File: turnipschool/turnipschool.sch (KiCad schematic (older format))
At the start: 45 parts, among them J1 GSG-900MHZ-F-ANTENNA, J2 GSG-USB-MICRO-B, P2 ANTENNA, P3 RESET_N, P4 DD, P5 DC, P6 3V3, P7 GND, P9 PWR, T1 BALUN, U1 CC1111, U2 AP7313, X1 CRYSTAL

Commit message: Add USB hub to TURNIPSCHOOL
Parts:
- removed J2: GSG-USB-MICRO-B, symbol GSG-USB-MICRO-B
- removed P9: PWR, symbol CONN_3X2
- added C15: 100uF, symbol C
- added C16: 100nF, symbol C
- added C17: 1uF, symbol C
- added C18, C19: 18pF, symbol C
- added J?: USB-DEVICE, symbol USB-DEVICE
- added P10, P11, P8, P9: CONN_1, symbol CONN_1
- added P8: GOODFET, symbol CONN_7X2
- added R14: 10k, symbol R
- added R15: 0, symbol R-SHORTED
- added R16, R17: 33, symbol R
- added R18, R19: 50k, symbol R
- added R20: 12k, symbol R
- added R21, R22, R23, R24: 100k, symbol R
- added U3: USB2412, symbol USB2412
- added U4: AP2511SN-7, symbol AP2511SN-7
- added X2: CRYSTAL, symbol CRYSTAL
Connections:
- net labels added: USBDM_DN2, USBDP_DN2
- wire segments 130 -> 189
- no-connect marks 1 -> 16
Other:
- note added: "programming header matching GoodFET pinout"
- moved on the sheet: C1, C10, C11, C12, C13, C14, C15, C16, C17, C2, C3, C4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

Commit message: Remove trace antenna, swap connector for pad
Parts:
- removed C6: 10nF, symbol C
- removed J1: GSG-900MHZ-F-ANTENNA, symbol GSG-900MHZ-F-ANTENNA
- removed P2: ANTENNA, symbol GSG-SMA-CONN
- added P13: CONN_1, symbol CONN_1
- C17: Note DNP -> (none)
- gave numbers to parts that had none: 1
- renumbered C15 to C20, C16 to C21, C17 to C22, P9 to P10, P10 to P11, P11 to P12, P8 to P9
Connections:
- wire segments 189 -> 181
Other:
- note added: "USB Cable"
- moved on the sheet: P10, P11, P12, P9

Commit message: Add changes suggestted by mossmann
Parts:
- removed C12, C13: 47pF, symbol C
- removed D1: TVS_DIODE, symbol GSG-DIODE-TVS-BI
- removed D3: LED2, symbol LED
- removed D4: LED3, symbol LED
- removed J2: USB-DEVICE, symbol USB-DEVICE
- removed P8: GOODFET, symbol CONN_7X2
- removed R11, R12: 330, symbol R
- removed R13, R15, R7: 0, symbol R-SHORTED
- removed R16, R17: 33, symbol R
- removed R6: 0, symbol R
- removed X1, X2: CRYSTAL, symbol CRYSTAL
- added C17, C18, C20, C22, C23, C24, C25: 100nF, symbol C
- added C27: 47uF, symbol C
- added FB1: FILTER, symbol FILTER
- added J2: USB-DEVICE-SHIELD, symbol USB-DEVICE-SHIELD
- added P11: CONN_1, symbol CONN_1
- added R7: 330, symbol R
- added X1, X2: CRYSTAL, symbol CRYSTAL_SMD
- C10, C11: value 22pF -> 10pF; Description CAP CER 22PF 50V 5% NP0 0402 -> CAP CER 10PF 50V 5% NP0 0402; Manufacturer Murata -> Kemet; Part Number GRM1555C1H220JA01D -> C0402C100J5GACTU
- C15: renamed from C18; value 18pF -> 6pF; Description (none) -> CAP CER 6PF 50V NP0 0402; Manufacturer (none) -> Samsung Electro-Mechanics America, Inc; Part Number (none) -> CL05C060DB5NCNC
- C16: renamed from C19; value 18pF -> 6pF; Description (none) -> CAP CER 6PF 50V NP0 0402; Manufacturer (none) -> Samsung Electro-Mechanics America, Inc; Part Number (none) -> CL05C060DB5NCNC
- C19: renamed from C22; Manufacturer (none) -> Taiyo Yuden
- C21: Description (none) -> CAP CER 0.1UF 10V 10% X5R 0402; Manufacturer (none) -> Murata; Part Number (none) -> GRM155R61A104KA01D
- C26: renamed from C20; value 100uF -> 100nF; Description (none) -> CAP CER 0.1UF 10V 10% X5R 0402; Manufacturer (none) -> Murata; Part Number (none) -> GRM155R61A104KA01D
- R10: renamed from R23; Description (none) -> RES 100K OHM 1/16W 5% 0402; Manufacturer (none) -> Samsung Electro-Mechanics America, Inc; Part Number (none) -> RC1005J104CS
- R11: renamed from R18; Description (none) -> RES 49.9K OHM 1/16W 1% 0402 SMD; Manufacturer (none) -> Rohm Semiconductor; Part Number (none) -> MCR01MRTF4992
- R12: renamed from R24; Description (none) -> RES 100K OHM 1/16W 5% 0402; Manufacturer (none) -> Samsung Electro-Mechanics America, Inc; Part Number (none) -> RC1005J104CS
- R13: renamed from R22; Description (none) -> RES 100K OHM 1/16W 5% 0402; Manufacturer (none) -> Samsung Electro-Mechanics America, Inc; Part Number (none) -> RC1005J104CS
- R14: renamed from R21; Description (none) -> RES 100K OHM 1/16W 5% 0402; Manufacturer (none) -> Samsung Electro-Mechanics America, Inc; Part Number (none) -> RC1005J104CS
- R15: renamed from R19; Description (none) -> RES 49.9K OHM 1/16W 1% 0402 SMD; Manufacturer (none) -> Rohm Semiconductor; Part Number (none) -> MCR01MRTF4992
- R8: value 1k5 -> 1M; Description RES 1.50K OHM 1/10W 1% 0603 SMD -> RES 1M OHM 1/16W 5% 0402; Manufacturer Rohm -> Samsung Electro-Mechanics America, Inc; Part Number MCR03ERTF1501 -> RC1005J105CS
- R9: renamed from R20; Description (none) -> RES 12K OHM 1/16W 1% 0402 SMD; Manufacturer (none) -> Rohm Semiconductor; Part Number (none) -> MCR01MRTF1202
- U3: Description (none) -> IC USB 2.0 HS HUB CTRLR 28QFN; Manufacturer (none) -> Microchip Technology; Part Number (none) -> USB2412-DZK
- U4: Description (none) -> USB POWER SWITCH U-DFN2020-6; Manufacturer (none) -> Diodes Incorporated; Part Number (none) -> AP2511SN-7
- renumbered C14 to C12, C15 to C13, C16 to C14, C4 to C3, C3 to C4, C17 to C6, P13 to P1, P12 to P10, P3 to P2, P4 to P3, P5 to P4, P6 to P5, P7 to P6, P9 to P7, P10 to P8, P11 to P9, R2 to R1, R4 to R2, R5 to R3, R9 to R4, R10 to R5, R14 to R6
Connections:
- net labels added: SHIELD
- net labels removed: P0_0, P0_1, P0_2, P0_3, P0_4, P1_2, P1_3, P1_4, P1_5, P1_6, P1_7, P2_3, P2_4
- wire segments 181 -> 164
- no-connect marks 16 -> 21
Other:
- note removed: "programming header matching GoodFET pinout"
- moved on the sheet: C11, C15, C16, C26, P2, P3, P4, P5, P6, R4, R5, R6

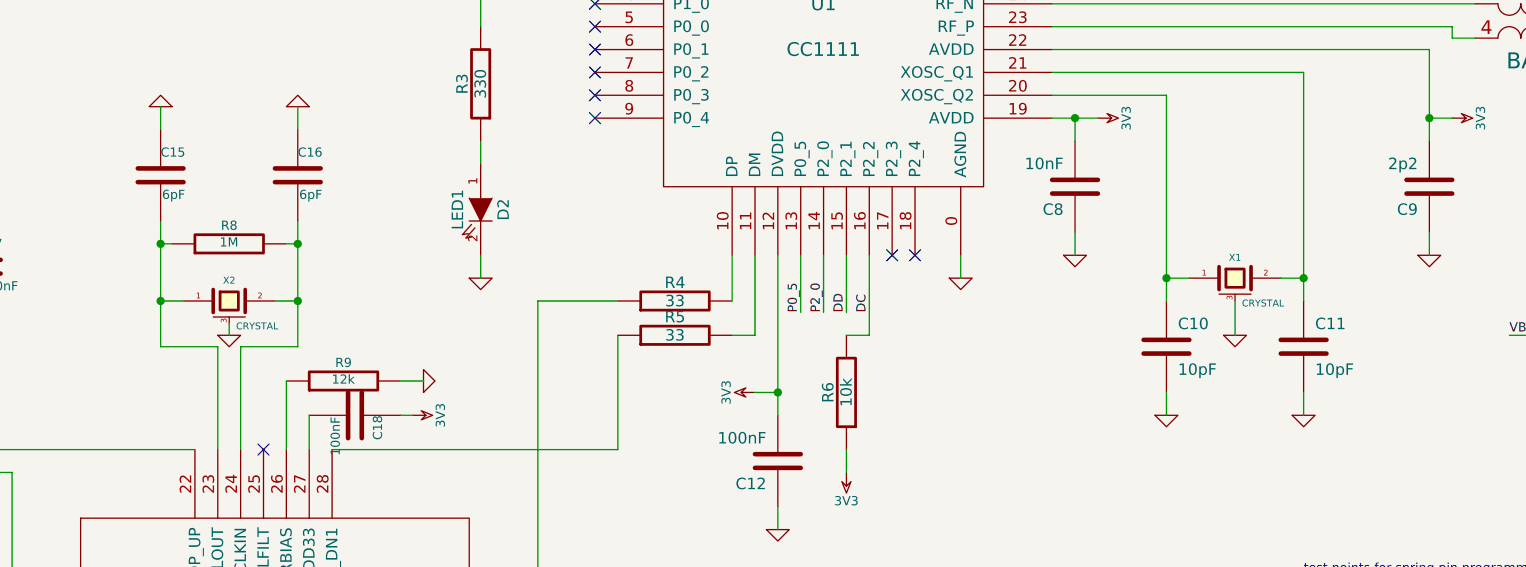
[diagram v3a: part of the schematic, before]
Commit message: Put crystal load capacitors back to sensible values (I shouldn't do late night maths)
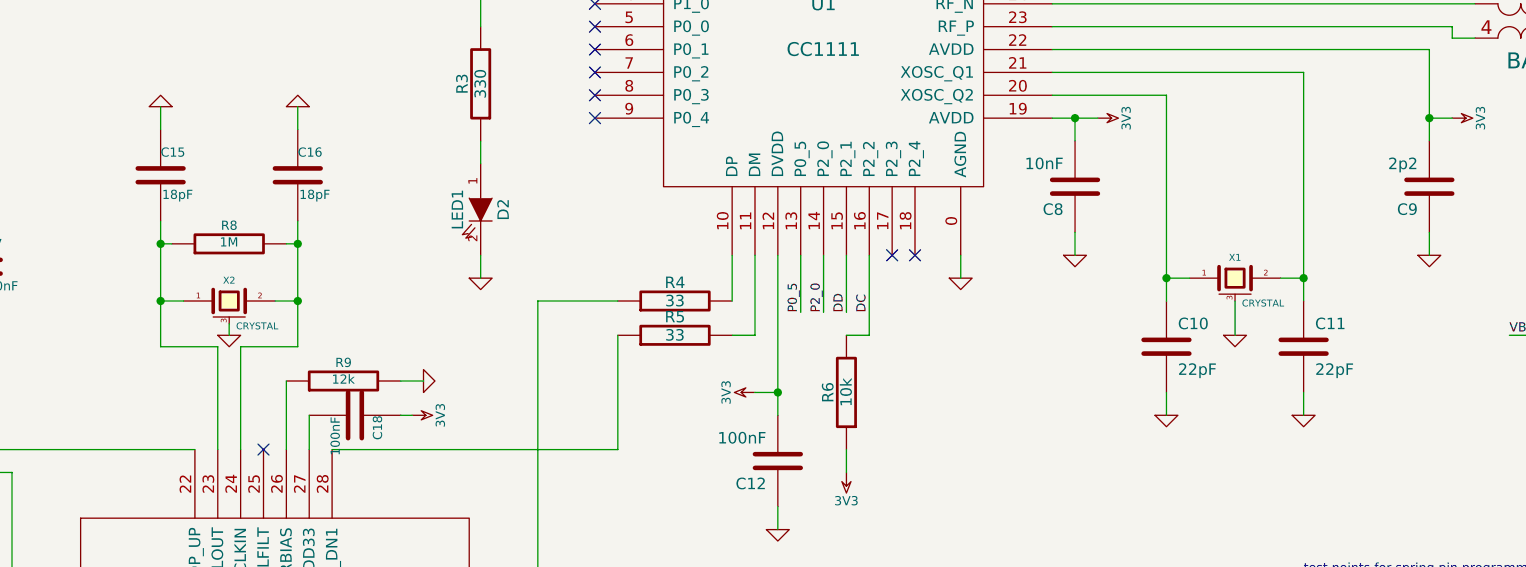
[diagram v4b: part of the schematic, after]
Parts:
- C10: value 10pF -> 22pF; Description CAP CER 10PF 50V 5% NP0 0402 -> (none); Manufacturer Kemet -> (none); Part Number C0402C100J5GACTU -> (none)
- C11: value 10pF -> 22pF; Description CAP CER 10PF 50V 5% NP0 0402 -> CAP CER 22PF 50V 5% NP0 0402; Manufacturer Kemet -> Samsung Electro-Mechanics America, Inc; Part Number C0402C100J5GACTU -> CL05C220JB5NNNC
- C15, C16: value 6pF -> 18pF; Description CAP CER 6PF 50V NP0 0402 -> CAP CER 18PF 50V 5% NP0 0402; Part Number CL05C060DB5NCNC -> CL05C180JB5NNNC
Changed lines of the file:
@@
 P 8150 4100
 F 0 "C11" H 8200 4200 50  0000 L CNN
-F 1 "10pF" H 8200 4000 50  0000 L CNN
+F 1 "22pF" H 8200 4000 50  0000 L CNN
 F 2 "" H 8150 4100 60  0001 C CNN
 F 3 "" H 8150 4100 60  0001 C CNN
-F 4 "Kemet" H 8150 4100 60  0001 C CNN "Manufacturer"
-F 5 "C0402C100J5GACTU" H 8150 4100 60  0001 C CNN "Part Number"
-F 6 "CAP CER 10PF 50V 5% NP0 0402" H 8150 4100 60  0001 C CNN "Description"
+F 4 "Samsung Electro-Mechanics America, Inc" H 8150 4100 60  0001 C CNN "Manufacturer"
+F 5 "CL05C220JB5NNNC" H 8150 4100 60  0001 C CNN "Part Number"
+F 6 "CAP CER 22PF 50V 5% NP0 0402" H 8150 4100 60  0001 C CNN "Description"
 	1    8150 4100
 	1    0    0    -1
@@
 P 7550 4100
 F 0 "C10" H 7600 4200 50  0000 L CNN
-F 1 "10pF" H 7600 4000 50  0000 L CNN
+F 1 "22pF" H 7600 4000 50  0000 L CNN
 F 2 "" H 7550 4100 60  0001 C CNN
 F 3 "" H 7550 4100 60  0001 C CNN
-F 4 "Kemet" H 7550 4100 60  0001 C CNN "Manufacturer"
-F 5 "C0402C100J5GACTU" H 7550 4100 60  0001 C CNN "Part Number"
-F 6 "CAP CER 10PF 50V 5% NP0 0402" H 7550 4100 60  0001 C CNN "Description"
 	1    7550 4100
 	1    0    0    -1
@@
 P 3150 3350
 F 0 "C15" H 3150 3450 40  0000 L CNN
-F 1 "6pF" H 3156 3265 40  0000 L CNN
+F 1 "18pF" H 3156 3265 40  0000 L CNN
 F 2 "" H 3188 3200 30  0000 C CNN
 F 3 "" H 3150 3350 60  0000 C CNN
 F 4 "Samsung Electro-Mechanics America, Inc" H 3150 3350 60  0001 C CNN "Manufacturer"
-F 5 "CL05C060DB5NCNC" H 3150 3350 60  0001 C CNN "Part Number"
-F 6 "CAP CER 6PF 50V NP0 0402" H 3150 3350 60  0001 C CNN "Description"
+F 5 "CL05C180JB5NNNC" H 3150 3350 60  0001 C CNN "Part Number"
+F 6 "CAP CER 18PF 50V 5% NP0 0402" H 3150 3350 60  0001 C CNN "Description"
 	1    3150 3350
 	1    0    0    -1
@@
 P 3750 3350
 F 0 "C16" H 3750 3450 40  0000 L CNN
-F 1 "6pF" H 3756 3265 40  0000 L CNN
+F 1 "18pF" H 3756 3265 40  0000 L CNN
 F 2 "" H 3788 3200 30  0000 C CNN
 F 3 "" H 3750 3350 60  0000 C CNN
 F 4 "Samsung Electro-Mechanics America, Inc" H 3750 3350 60  0001 C CNN "Manufacturer"
-F 5 "CL05C060DB5NCNC" H 3750 3350 60  0001 C CNN "Part Number"
-F 6 "CAP CER 6PF 50V NP0 0402" H 3750 3350 60  0001 C CNN "Description"
+F 5 "CL05C180JB5NNNC" H 3750 3350 60  0001 C CNN "Part Number"
+F 6 "CAP CER 18PF 50V 5% NP0 0402" H 3750 3350 60  0001 C CNN "Description"
 	1    3750 3350
 	1    0    0    -1
@@
 Connection ~ 8150 3800
 $Comp
-L GND #PWR?
+L GND #PWR055
 U 1 1 5394E864
 P 7850 4050
-F 0 "#PWR?" H 7850 4050 30  0001 C CNN
+F 0 "#PWR055" H 7850 4050 30  0001 C CNN
 F 1 "GND" H 7850 3980 30  0001 C CNN
 F 2 "" H 7850 4050 60  0000 C CNN
@@
 Connection ~ 3150 3900
 $Comp
-L GND #PWR?
+L GND #PWR056
 U 1 1 5394EEC8
 P 3450 4050
-F 0 "#PWR?" H 3450 4050 30  0001 C CNN
+F 0 "#PWR056" H 3450 4050 30  0001 C CNN
 F 1 "GND" H 3450 3980 30  0001 C CNN
 F 2 "" H 3450 4050 60  0000 C CNN

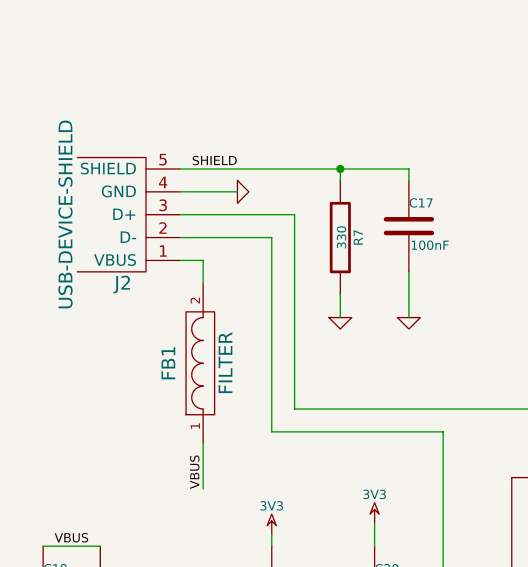
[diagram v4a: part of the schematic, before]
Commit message: All parts are now 0402s where possible.
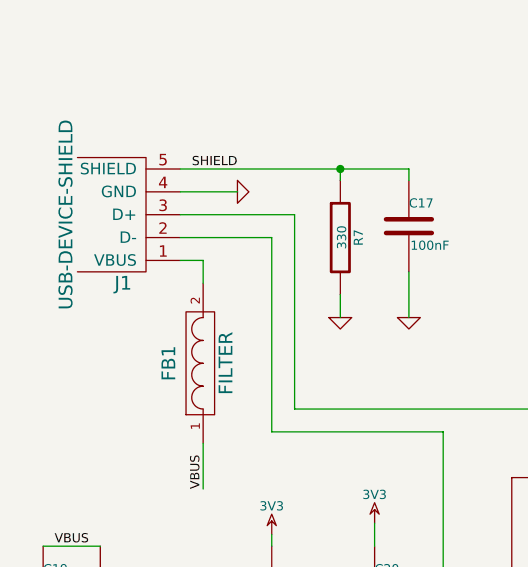
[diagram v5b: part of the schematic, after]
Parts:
- C1, C13: Description CAP CER 1UF 10V 10% X7R 0603 -> CAP CER 1UF 6.3V 5% X5R 0402; Manufacturer Taiyo Yuden -> Samsung Electro-Mechanics America, Inc; Part Number LMK107B7105KA-T -> CL05A105JQ5NNNC
- C10: Description (none) -> CAP CER 22PF 50V 5% NP0 0402; Manufacturer (none) -> Samsung Electro-Mechanics America, Inc; Part Number (none) -> CL05C220JB5NNNC
- C14: Description CAP CER 4.7UF 6.3V 10% X5R 0603 -> CAP CER 4.7UF 6.3V 20% X5R 0402; Manufacturer Taiyo Yuden -> Samsung Electro-Mechanics America, Inc; Part Number JMK107BJ475KA-T -> CL05A475MQ5NRNC
- C19: Description (none) -> CAP CER 1UF 6.3V 5% X5R 0402; Manufacturer Taiyo Yuden -> Samsung Electro-Mechanics America, Inc; Part Number (none) -> CL05A105JQ5NNNC
- C6: Description CAP CER 10000PF 50V 10% X7R 0603 -> CAP CER 10000PF 16V 10% X7R 0402; Manufacturer Murata -> Samsung Electro-Mechanics America, Inc; Part Number GRM188R71H103KA01D -> CL05B103KO5NCNC
- D2: Description LED CHIPLED 570NM GREEN 0603 SMD -> LED GREEN 0.2MM 13MCD 0402 SMD; Manufacturer OSRAM -> Rohm; Part Number LG Q971-KN-1 -> SML-P12PTT86
- J1: renamed from J2; Description (none) -> CONN PLUG USB A-TYPE SMD; Manufacturer (none) -> Keystone Electronics; Part Number (none) -> 931
- R1, R6: Description RES 10K OHM 1/10W 5% 0603 SMD -> RES 10.0K OHM 1/16W 5% 0402; Manufacturer Stackpole -> TE Connectivity; Part Number RMCF0603JT10K0 -> 1622826-4
- R3, R7: Description RES 330 OHM 1/10W 5% 0603 SMD -> RES 330 OHM 1/16W 5% 0402; Manufacturer Stackpole -> Samsung Electro-Mechanics America, Inc; Part Number RMCF0603JT330R -> RC1005J331CS
- R4, R5: Description RES 33.0 OHM 1/10W 1% 0603 SMD -> RES 33 OHM 1/16W 5% 0402; Manufacturer Rohm -> Samsung Electro-Mechanics America, Inc; Part Number MCR03ERTF33R0 -> RC1005J330CS
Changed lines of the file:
@@
 encoding utf-8
 Sheet 1 1
-Title ""
-Date "19 oct 2012"
+Title "TURNIPSCHOOL"
+Date "09 Jun 2014"
 Rev ""
-Comp ""
-Comment1 ""
+Comp "Copyright 2014 Dominic Spill, Michael Ossmann"
+Comment1 "License: GPL v2"
 Comment2 ""
 Comment3 ""
@@
 F 2 "" H 9900 2600 60  0001 C CNN
 F 3 "" H 9900 2600 60  0001 C CNN
-F 4 "Murata" H 9900 2600 60  0001 C CNN "Manufacturer"
-F 5 "GRM188R71H103KA01D" H 9900 2600 60  0001 C CNN "Part Number"
-F 6 "CAP CER 10000PF 50V 10% X7R 0603" H 9900 2600 60  0001 C CNN "Description"
+F 4 "Samsung Electro-Mechanics America, Inc" H 9900 2600 60  0001 C CNN "Manufacturer"
+F 5 "CL05B103KO5NCNC" H 9900 2600 60  0001 C CNN "Part Number"
+F 6 "CAP CER 10000PF 16V 10% X7R 0402" H 9900 2600 60  0001 C CNN "Description"
 	1    9900 2600
 	0    1    1    0
@@
 F 2 "" H 4550 2950 60  0001 C CNN
 F 3 "" H 4550 2950 60  0001 C CNN
-F 4 "Stackpole" H 4550 2950 60  0001 C CNN "Manufacturer"
-F 5 "RMCF0603JT330R" H 4550 2950 60  0001 C CNN "Part Number"
-F 6 "RES 330 OHM 1/10W 5% 0603 SMD" H 4550 2950 60  0001 C CNN "Description"
+F 4 "Samsung Electro-Mechanics America, Inc" H 4550 2950 60  0001 C CNN "Manufacturer"
+F 5 "RC1005J331CS" H 4550 2950 60  0001 C CNN "Part Number"
+F 6 "RES 330 OHM 1/16W 5% 0402" H 4550 2950 60  0001 C CNN "Description"
 	1    4550 2950
 	-1   0    0    1
@@
 F 2 "" H 4550 3500 60  0001 C CNN
 F 3 "" H 4550 3500 60  0001 C CNN
-F 4 "OSRAM" H 4550 3500 60  0001 C CNN "Manufacturer"
-F 5 "LG Q971-KN-1" H 4550 3500 60  0001 C CNN "Part Number"
-F 6 "LED CHIPLED 570NM GREEN 0603 SMD" H 4550 3500 60  0001 C CNN "Description"
+F 4 "Rohm" H 4550 3500 60  0001 C CNN "Manufacturer"
+F 5 "SML-P12PTT86" H 4550 3500 60  0001 C CNN "Part Number"
+F 6 "LED GREEN 0.2MM 13MCD 0402 SMD" H 4550 3500 60  0001 C CNN "Description"
 	1    4550 3500
 	0    1    1    0
@@
 F 2 "" H 6000 1050 60  0001 C CNN
 F 3 "" H 6000 1050 60  0001 C CNN
-F 4 "Stackpole" H 6000 1050 60  0001 C CNN "Manufacturer"
-F 5 "RMCF0603JT10K0" H 6000 1050 60  0001 C CNN "Part Number"
-F 6 "RES 10K OHM 1/10W 5% 0603 SMD" H 6000 1050 60  0001 C CNN "Description"
+F 4 "TE Connectivity" H 6000 1050 60  0001 C CNN "Manufacturer"
+F 5 "1622826-4" H 6000 1050 60  0001 C CNN "Part Number"
+F 6 "RES 10.0K OHM 1/16W 5% 0402" H 6000 1050 60  0001 C CNN "Description"
 	1    6000 1050
 	-1   0    0    1
@@
 F 2 "" H 9800 4450 60  0001 C CNN
 F 3 "" H 9800 4450 60  0001 C CNN
-F 4 "Taiyo Yuden" H 9800 4450 60  0001 C CNN "Manufacturer"
-F 5 "JMK107BJ475KA-T" H 9800 4450 60  0001 C CNN "Part Number"
-F 6 "CAP CER 4.7UF 6.3V 10% X5R 0603" H 9800 4450 60  0001 C CNN "Description"
+F 4 "Samsung Electro-Mechanics America, Inc" H 9800 4450 60  0001 C CNN "Manufacturer"
+F 5 "CL05A475MQ5NRNC" H 9800 4450 60  0001 C CNN "Part Number"
+F 6 "	CAP CER 4.7UF 6.3V 20% X5R 0402" H 9800 4450 60  0001 C CNN "Description"
 	1    9800 4450
 	1    0    0    -1
@@
 F 2 "" H 9300 4350 60  0001 C CNN
 F 3 "" H 9300 4350 60  0001 C CNN
-F 4 "Taiyo Yuden" H 9300 4350 60  0001 C CNN "Manufacturer"
-F 5 "LMK107B7105KA-T" H 9300 4350 60  0001 C CNN "Part Number"
-F 6 "CAP CER 1UF 10V 10% X7R 0603" H 9300 4350 60  0001 C CNN "Description"
+F 4 "Samsung Electro-Mechanics America, Inc" H 9300 4350 60  0001 C CNN "Manufacturer"
+F 5 "CL05A105JQ5NNNC" H 9300 4350 60  0001 C CNN "Part Number"
+F 6 "CAP CER 1UF 6.3V 5% X5R 0402" H 9300 4350 60  0001 C CNN "Description"
 	1    9300 4350
 	1    0    0    -1
@@
 F 2 "" H 6250 950 60  0001 C CNN
 F 3 "" H 6250 950 60  0001 C CNN
-F 4 "Taiyo Yuden" H 6250 950 60  0001 C CNN "Manufacturer"
-F 5 "LMK107B7105KA-T" H 6250 950 60  0001 C CNN "Part Number"
-F 6 "CAP CER 1UF 10V 10% X7R 0603" H 6250 950 60  0001 C CNN "Description"
+F 4 "Samsung Electro-Mechanics America, Inc" H 6250 950 60  0001 C CNN "Manufacturer"
+F 5 "CL05A105JQ5NNNC" H 6250 950 60  0001 C CNN "Part Number"
+F 6 "CAP CER 1UF 6.3V 5% X5R 0402" H 6250 950 60  0001 C CNN "Description"
 	1    6250 950
 	1    0    0    -1
@@
 F 2 "" H 7550 4100 60  0001 C CNN
 F 3 "" H 7550 4100 60  0001 C CNN
+F 4 "Samsung Electro-Mechanics America, Inc" H 7550 4100 60  0001 C CNN "Manufacturer"
+F 5 "CL05C220JB5NNNC" H 7550 4100 60  0001 C CNN "Part Number"
+F 6 "CAP CER 22PF 50V 5% NP0 0402" H 7550 4100 60  0001 C CNN "Description"
 	1    7550 4100
 	1    0    0    -1
@@
 F 2 "" H 6150 4300 60  0001 C CNN
 F 3 "" H 6150 4300 60  0001 C CNN
-F 4 "Stackpole" H 6150 4300 60  0001 C CNN "Manufacturer"
-F 5 "RMCF0603JT10K0" H 6150 4300 60  0001 C CNN "Part Number"
-F 6 "RES 10K OHM 1/10W 5% 0603 SMD" H 6150 4300 60  0001 C CNN "Description"
+F 4 "TE Connectivity" H 6150 4300 60  0001 C CNN "Manufacturer"
+F 5 "1622826-4" H 6150 4300 60  0001 C CNN "Part Number"
+F 6 "RES 10.0K OHM 1/16W 5% 0402" H 6150 4300 60  0001 C CNN "Description"
 	1    6150 4300
 	-1   0    0    1
@@
 F 2 "" H 788 5200 30  0000 C CNN
 F 3 "" H 750 5350 60  0000 C CNN
-F 4 "Taiyo Yuden" H 750 5350 60  0001 C CNN "Manufacturer"
+F 4 "Samsung Electro-Mechanics America, Inc" H 750 5350 60  0001 C CNN "Manufacturer"
+F 5 "CL05A105JQ5NNNC" H 750 5350 60  0001 C CNN "Part Number"
+F 6 "CAP CER 1UF 6.3V 5% X5R 0402" H 750 5350 60  0001 C CNN "Description"
 	1    750  5350
 	1    0    0    -1
@@
 $EndComp
 $Comp
-L USB-DEVICE-SHIELD J2
+L USB-DEVICE-SHIELD J1
 U 1 1 539201B4
 P 1150 3700
-F 0 "J2" H 1200 4000 60  0000 C CNN
+F 0 "J1" H 1200 4000 60  0000 C CNN
 F 1 "USB-DEVICE-SHIELD" V 1450 3700 60  0000 C CNN
 F 2 "" H 1150 3750 60  0000 C CNN
 F 3 "" H 1150 3750 60  0000 C CNN
+F 4 "Keystone Electronics" H 1150 3700 60  0001 C CNN "Manufacturer"
+F 5 "931" H 1150 3700 60  0001 C CNN "Part Number"
+F 6 "CONN PLUG USB A-TYPE SMD" H 1150 3700 60  0001 C CNN "Description"
 	1    1150 3700
 	-1   0    0    1
@@
 F 2 "" V 1980 3800 30  0000 C CNN
 F 3 "" H 2050 3800 30  0000 C CNN
-F 4 "Stackpole" H 2050 3800 60  0001 C CNN "Manufacturer"
-F 5 "RMCF0603JT330R" H 2050 3800 60  0001 C CNN "Part Number"
-F 6 "RES 330 OHM 1/10W 5% 0603 SMD" H 2050 3800 60  0001 C CNN "Description"
+F 4 "Samsung Electro-Mechanics America, Inc" H 2050 3800 60  0001 C CNN "Manufacturer"
+F 5 "RC1005J331CS" H 2050 3800 60  0001 C CNN "Part Number"
+F 6 "RES 330 OHM 1/16W 5% 0402" H 2050 3800 60  0001 C CNN "Description"
 	1    2050 3800
 	1    0    0    -1
@@
 F 2 "" H 5400 4050 60  0001 C CNN
 F 3 "" H 5400 4050 60  0001 C CNN
-F 4 "Rohm" H 5400 4050 60  0001 C CNN "Manufacturer"
-F 5 "MCR03ERTF33R0" H 5400 4050 60  0001 C CNN "Part Number"
-F 6 "RES 33.0 OHM 1/10W 1% 0603 SMD" H 5400 4050 60  0001 C CNN "Description"
+F 4 "Samsung Electro-Mechanics America, Inc" H 5400 4050 60  0001 C CNN "Manufacturer"
+F 5 "RC1005J330CS" H 5400 4050 60  0001 C CNN "Part Number"
+F 6 "RES 33 OHM 1/16W 5% 0402" H 5400 4050 60  0001 C CNN "Description"
 	1    5400 4050
 	0    -1   -1   0
@@
 F 2 "" H 5400 3900 60  0001 C CNN
 F 3 "" H 5400 3900 60  0001 C CNN
-F 4 "Rohm" H 5400 3900 60  0001 C CNN "Manufacturer"
-F 5 "MCR03ERTF33R0" H 5400 3900 60  0001 C CNN "Part Number"
-F 6 "RES 33.0 OHM 1/10W 1% 0603 SMD" H 5400 3900 60  0001 C CNN "Description"
+F 4 "Samsung Electro-Mechanics America, Inc" H 5400 3900 60  0001 C CNN "Manufacturer"
+F 5 "RC1005J330CS" H 5400 3900 60  0001 C CNN "Part Number"
+F 6 "RES 33 OHM 1/16W 5% 0402" H 5400 3900 60  0001 C CNN "Description"
 	1    5400 3900
 	0    -1   -1   0
